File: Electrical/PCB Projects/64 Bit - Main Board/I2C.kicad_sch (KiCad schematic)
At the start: 22 parts, among them U2 PCA9306, U3 DS1307+, U8 24LC64, Y3 32.768kHz-12.6pF

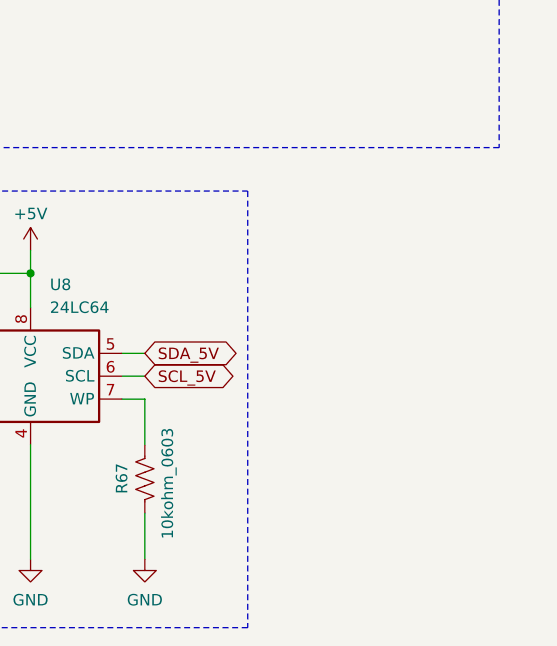
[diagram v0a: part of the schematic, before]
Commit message: added I2C ambient light sensor
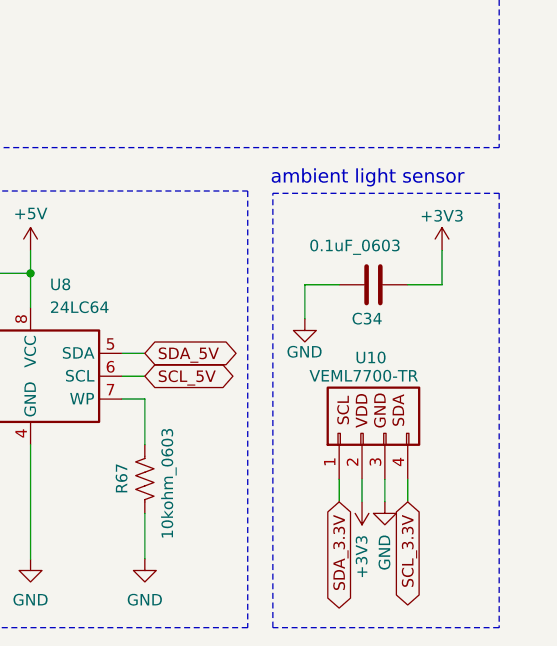
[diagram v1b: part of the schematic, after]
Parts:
- added C34: 0.1uF_0603, Capacitor_SMD:C_0603_1608Metric, symbol Device:C
- added U10: VEML7700-TR, Footprint drive Dump 1:VEML7700, symbol Connector_Generic:Conn_01x04
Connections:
- net +3V3: now also C34.2, U10.2 (VDD)
- net GND: now also C34.1, U10.3 (GND)
- net SCL_3.3V: now also U10.4 (SDA)
- net SDA_3.3V: now also U10.1 (SCL)
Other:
- note added: "ambient light sensor"

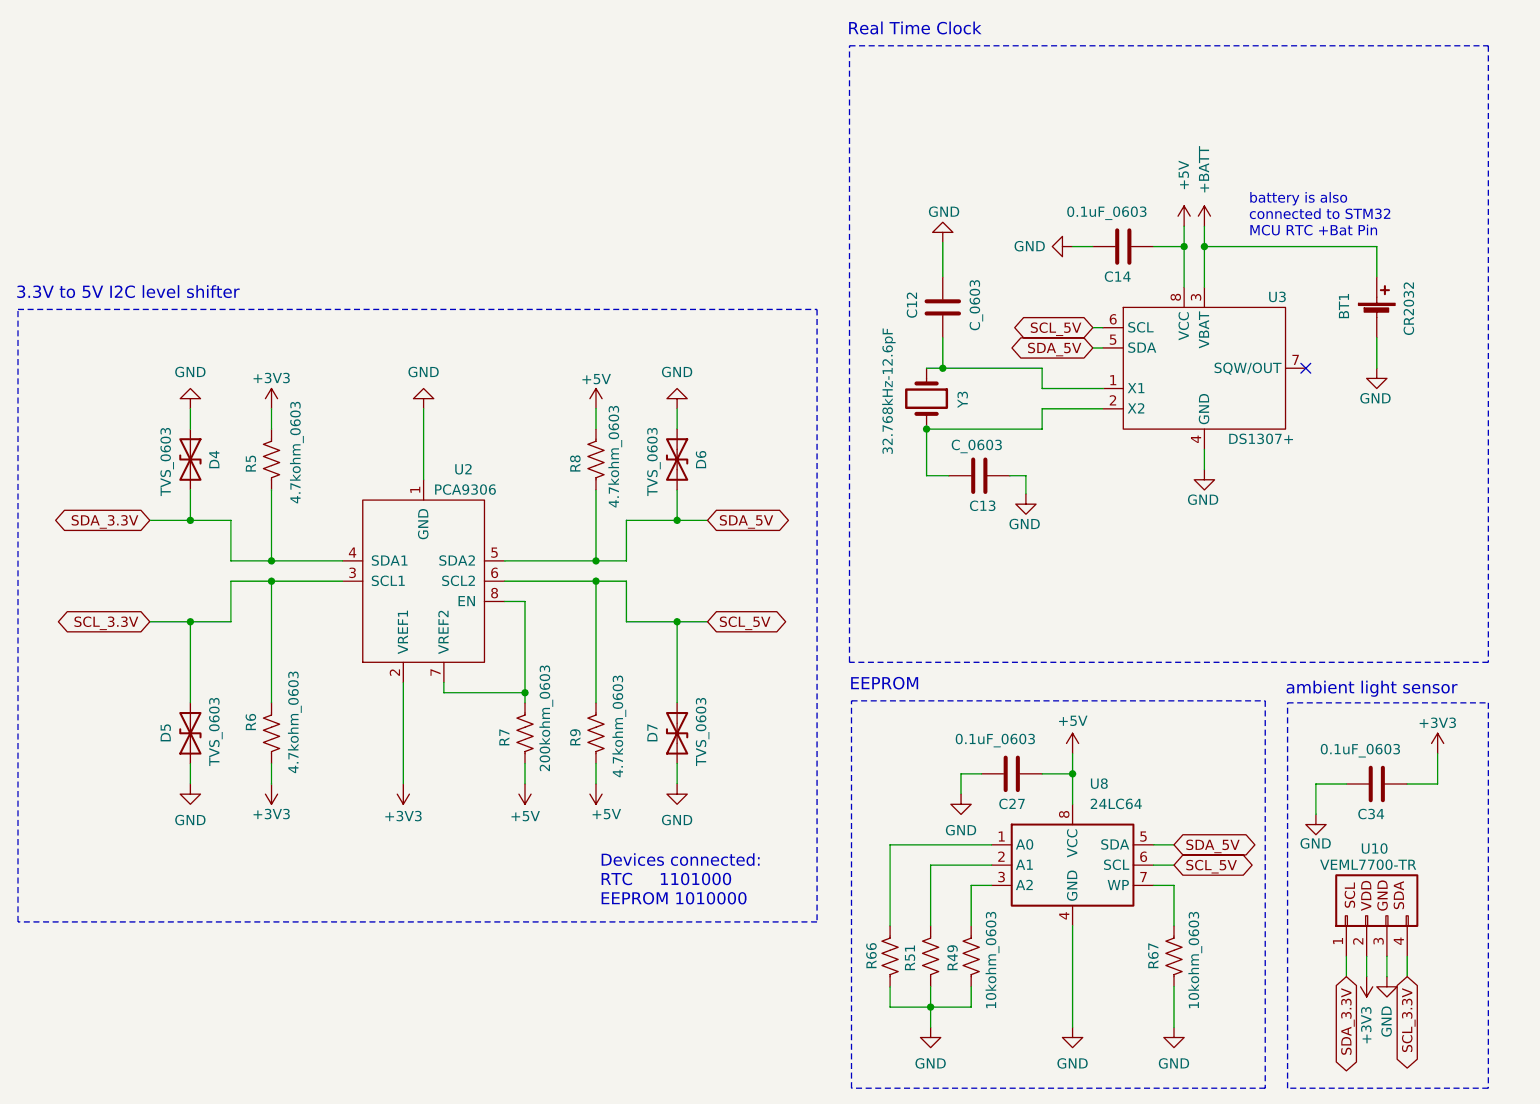
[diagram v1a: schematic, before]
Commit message: near final state. Includes BOM, price, etc
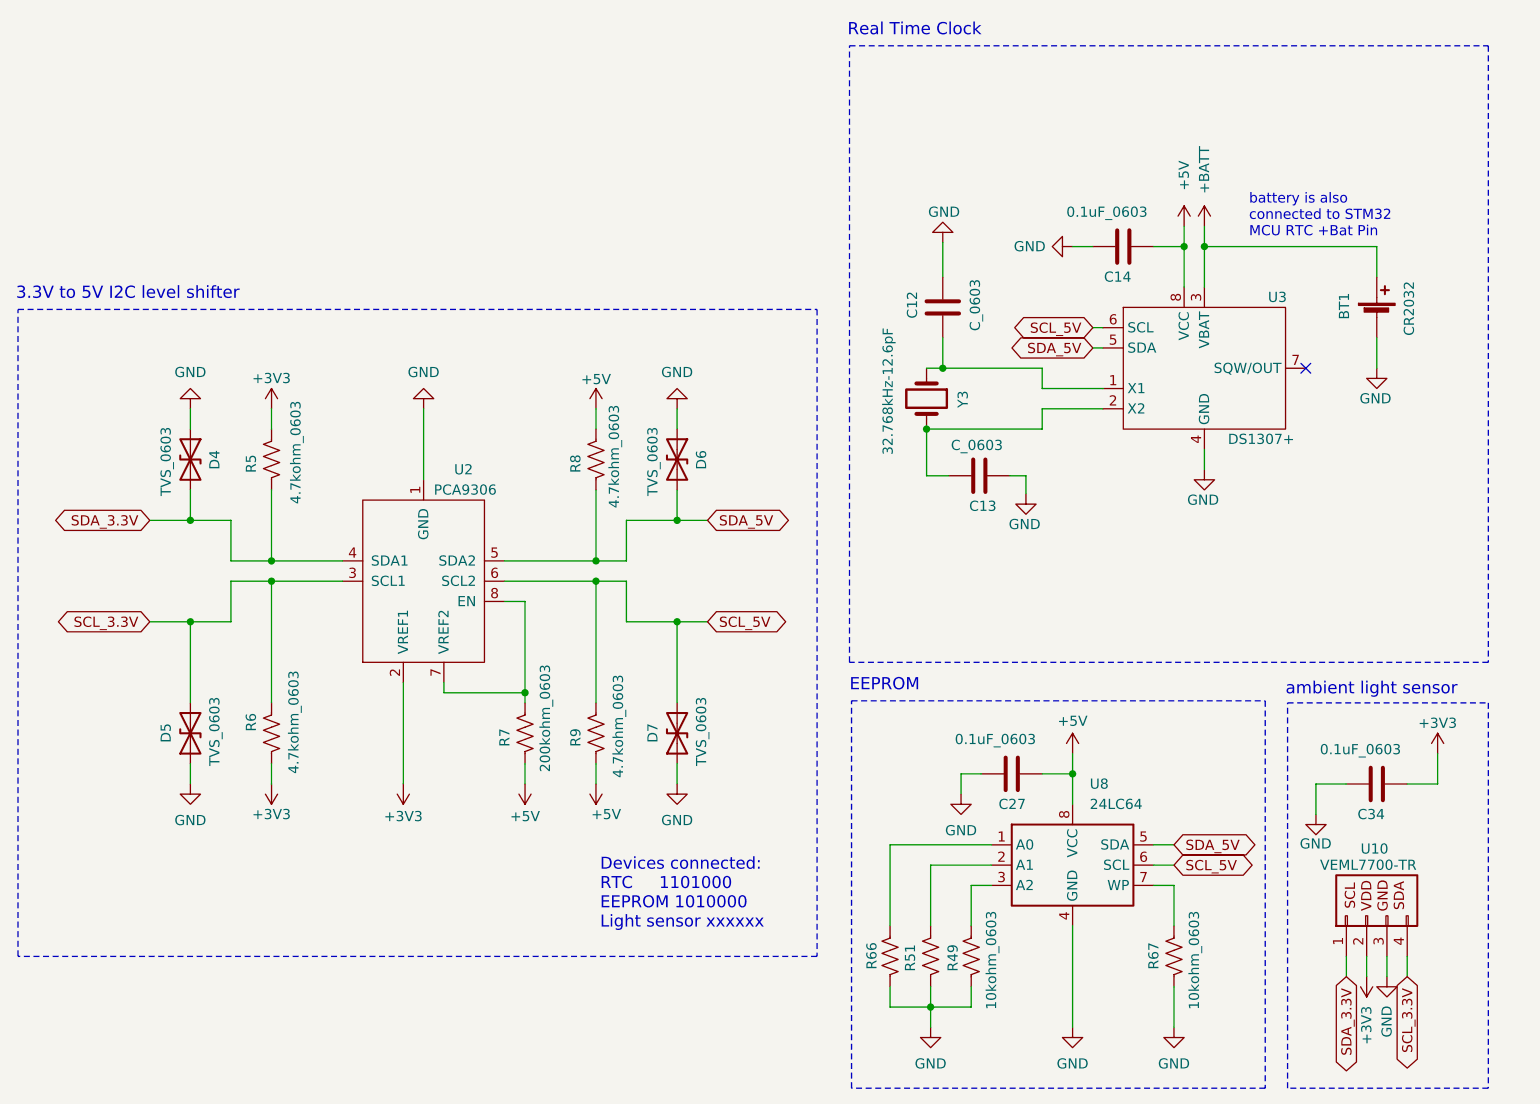
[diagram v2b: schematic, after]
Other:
- note added: "Devices connected: RTC 1101000 EEPROM 1010000 Light sensor xxxxxx"
- note removed: "Devices connected: RTC 1101000 EEPROM 1010000"
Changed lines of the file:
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@@
 	(title_block
 		(title "RTC & RTC Level Shifting")
-		(date "2025-OCT-04")
+		(date "2025-12-01")
 		(rev "1")
 		(company "Kadin Whiting")
@@
 	(rectangle
 		(start 59.69 58.674)
-		(end 159.766 135.382)
+		(end 159.766 139.7)
 		(stroke
 			(width 0)
@@
 		)
 	)
-	(text "Devices connected:\nRTC     1101000\nEEPROM 1010000"
+	(text "Devices connected:\nRTC     1101000\nEEPROM 1010000\nLight sensor xxxxxx"
 		(exclude_from_sim no)
-		(at 132.588 133.604 0)
+		(at 132.588 136.398 0)
 		(effects
 			(font

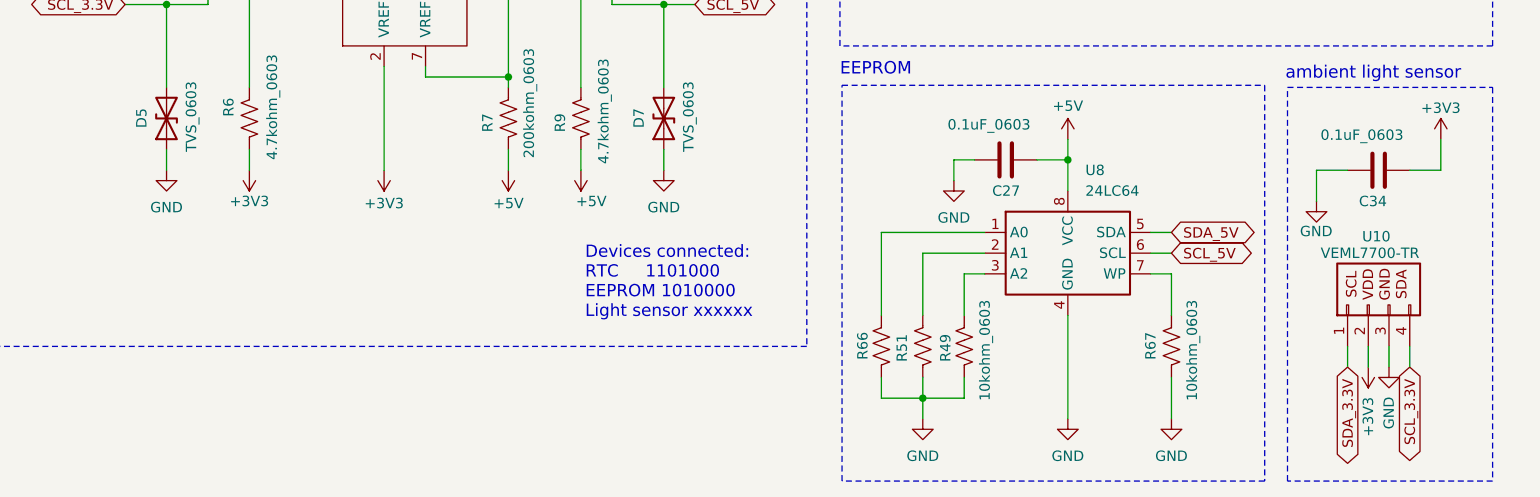
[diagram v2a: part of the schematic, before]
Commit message: final. PCB outputs generated, ordering prototypes
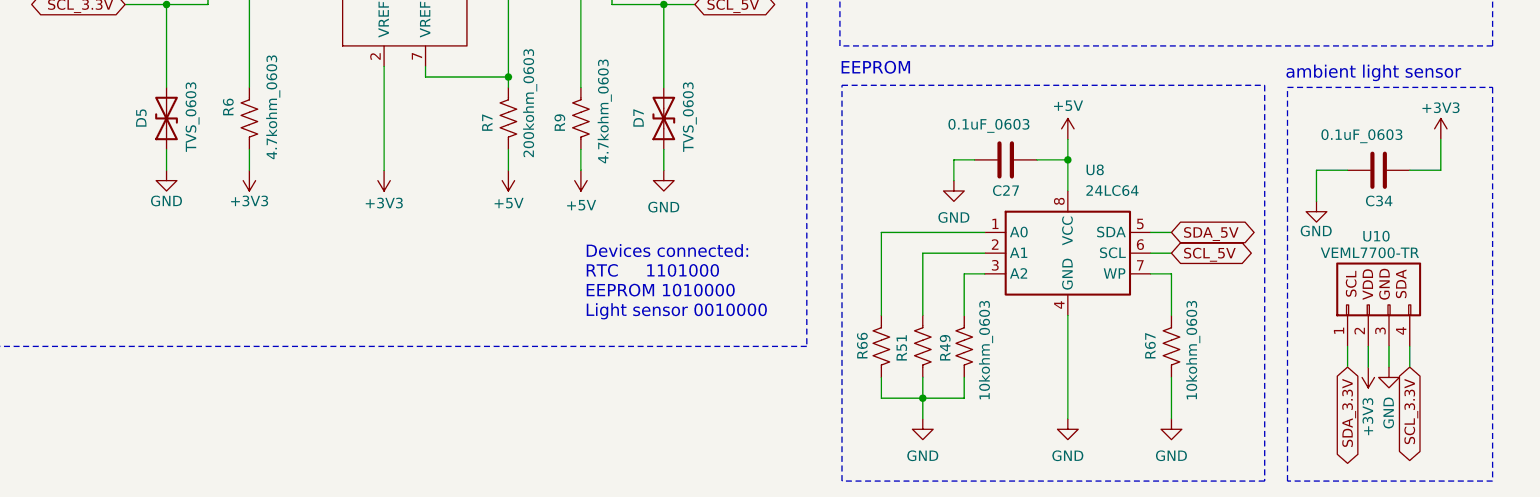
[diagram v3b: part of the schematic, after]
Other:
- note added: "Devices connected: RTC 1101000 EEPROM 1010000 Light sensor 0010000"
- note removed: "Devices connected: RTC 1101000 EEPROM 1010000 Light sensor xxxxxx"
